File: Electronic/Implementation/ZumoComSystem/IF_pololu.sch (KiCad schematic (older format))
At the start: 35 parts, among them J4 Pin-Header 2x13, J5 Conn_02x07_Odd_Even, J6 Pin-Header 2x13, J7 Conn_02x07_Odd_Even, Q10 SI2302CDS-T1-BE3, Q6 SI2302CDS-T1-BE3, Q7 SI2302CDS-T1-BE3, Q8 SI2302CDS-T1-BE3, Q9 SI2302CDS-T1-BE3, SW3 KMR221GLFS, SW4 KMR221GLFS, SW5 KMR221GLFS

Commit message: #93 small fixes
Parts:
- D11: Manufacturer (none) -> Broadcom Limited; Part-No. (none) -> HSMF-C118
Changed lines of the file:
@@
 Sheet 7 7
 Title "Zumo Communication System"
-Date "2022-08-04"
+Date "2022-08-05"
 Rev "V1.1"
 Comp "NewTec GmbH"
@@
 F 2 "footprints:LED_RGB_1210" H 2800 6850 50  0001 C CNN
 F 3 "https://docs.broadcom.com/doc/AV02-0610EN" H 2800 6850 50  0001 C CNN
+F 4 "Broadcom Limited" H 2800 6900 50  0001 C CNN "Manufacturer"
+F 5 "HSMF-C118" H 2800 6900 50  0001 C CNN "Part-No."
 	1    2800 6900
 	1    0    0    -1

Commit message: #95 Anode of State-LED (D11) with 3V3 instead 5V connected
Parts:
- R28, R29: value 150 -> 100; Part-No. RC0603FR-07150RL -> RT0603FRE07100RL
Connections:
- net +3V3: now also D11.1 (A)
- net +5V: no longer D11.1 (A)
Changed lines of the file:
@@
 Sheet 7 7
 Title "Zumo Communication System"
-Date "2022-09-07"
+Date "2022-09-12"
 Rev "V1.2"
 Comp "NewTec GmbH"
@@
 Text HLabel 1400 7250 0    50   Input ~ 0
 nRGB_LED_B
-$Comp
-L Device:R R28
-U 1 1 61002789
-P 2100 6900
-F 0 "R28" V 1893 6900 50  0000 C CNN
-F 1 "150" V 1984 6900 50  0000 C CNN
-F 2 "Resistor_SMD:R_0603_1608Metric_Pad1.05x0.95mm_HandSolder" V 2030 6900 50  0001 C CNN
-F 3 "~" H 2100 6900 50  0001 C CNN
-F 4 "YAGEO" H 2100 6900 50  0001 C CNN "Manufacturer"
-F 5 "RC0603FR-07150RL" H 2100 6900 50  0001 C CNN "Part-No."
-	1    2100 6900
-	0    1    1    0
-$EndComp
-$Comp
-L Device:R R29
-U 1 1 61002936
-P 2100 7250
-F 0 "R29" V 1893 7250 50  0000 C CNN
-F 1 "150" V 1984 7250 50  0000 C CNN
-F 2 "Resistor_SMD:R_0603_1608Metric_Pad1.05x0.95mm_HandSolder" V 2030 7250 50  0001 C CNN
-F 3 "~" H 2100 7250 50  0001 C CNN
-F 4 "YAGEO" H 2100 7250 50  0001 C CNN "Manufacturer"
-F 5 "RC0603FR-07150RL" H 2100 7250 50  0001 C CNN "Part-No."
-	1    2100 7250
-	0    1    1    0
-$EndComp
 Wire Wire Line
 	2250 6550 2450 6550
@@
 $EndComp
 $Comp
-L power:+5V #PWR061
-U 1 1 6222DB21
-P 3250 6500
-F 0 "#PWR061" H 3250 6350 50  0001 C CNN
-F 1 "+5V" H 3265 6673 50  0000 C CNN
-F 2 "" H 3250 6500 50  0001 C CNN
-F 3 "" H 3250 6500 50  0001 C CNN
-	1    3250 6500
-	1    0    0    -1
-$EndComp
-$Comp
 L power:+5V #PWR072
 U 1 1 62267367
@@
 Wire Wire Line
 	2250 6900 2600 6900
-$Comp
-L Device:R R27
-U 1 1 61001F8A
-P 2100 6550
-F 0 "R27" V 1893 6550 50  0000 C CNN
-F 1 "300" V 1984 6550 50  0000 C CNN
-F 2 "Resistor_SMD:R_0603_1608Metric_Pad1.05x0.95mm_HandSolder" V 2030 6550 50  0001 C CNN
-F 3 "~" H 2100 6550 50  0001 C CNN
-F 4 "Bourns Inc." H 2100 6550 50  0001 C CNN "Manufacturer"
-F 5 "CR0603-JW-301ELF" H 2100 6550 50  0001 C CNN "Part-No."
-	1    2100 6550
-	0    1    1    0
-$EndComp
 Text Notes 5950 4150 0    50   ~ 0
 I_max = 2.6 A
@@
 Text Notes 9150 3200 0    50   ~ 0
 right
+$Comp
+L power:+3.3V #PWR?
+U 1 1 6320421B
+P 3250 6500
+F 0 "#PWR?" H 3250 6350 50  0001 C CNN
+F 1 "+3.3V" H 3265 6673 50  0000 C CNN
+F 2 "" H 3250 6500 50  0001 C CNN
+F 3 "" H 3250 6500 50  0001 C CNN
+	1    3250 6500
+	1    0    0    -1
+$EndComp
+$Comp
+L Device:R R27
+U 1 1 61001F8A
+P 2100 6550
+F 0 "R27" V 1893 6550 50  0000 C CNN
+F 1 "300" V 1984 6550 50  0000 C CNN
+F 2 "Resistor_SMD:R_0603_1608Metric_Pad1.05x0.95mm_HandSolder" V 2030 6550 50  0001 C CNN
+F 3 "~" H 2100 6550 50  0001 C CNN
+F 4 "Bourns Inc." H 2100 6550 50  0001 C CNN "Manufacturer"
+F 5 "CR0603-JW-301ELF" H 2100 6550 50  0001 C CNN "Part-No."
+	1    2100 6550
+	0    1    1    0
+$EndComp
+$Comp
+L Device:R R29
+U 1 1 61002936
+P 2100 7250
+F 0 "R29" V 1893 7250 50  0000 C CNN
+F 1 "100" V 1984 7250 50  0000 C CNN
+F 2 "Resistor_SMD:R_0603_1608Metric_Pad1.05x0.95mm_HandSolder" V 2030 7250 50  0001 C CNN
+F 3 "~" H 2100 7250 50  0001 C CNN
+F 4 "YAGEO" H 2100 7250 50  0001 C CNN "Manufacturer"
+F 5 "RT0603FRE07100RL" H 2100 7250 50  0001 C CNN "Part-No."
+	1    2100 7250
+	0    1    1    0
+$EndComp
+$Comp
+L Device:R R28
+U 1 1 61002789
+P 2100 6900
+F 0 "R28" V 1893 6900 50  0000 C CNN
+F 1 "100" V 1984 6900 50  0000 C CNN
+F 2 "Resistor_SMD:R_0603_1608Metric_Pad1.05x0.95mm_HandSolder" V 2030 6900 50  0001 C CNN
+F 3 "~" H 2100 6900 50  0001 C CNN
+F 4 "YAGEO" H 2100 6900 50  0001 C CNN "Manufacturer"
+F 5 "RT0603FRE07100RL" H 2100 6900 50  0001 C CNN "Part-No."
+	1    2100 6900
+	0    1    1    0
+$EndComp
 $EndSCHEMATC

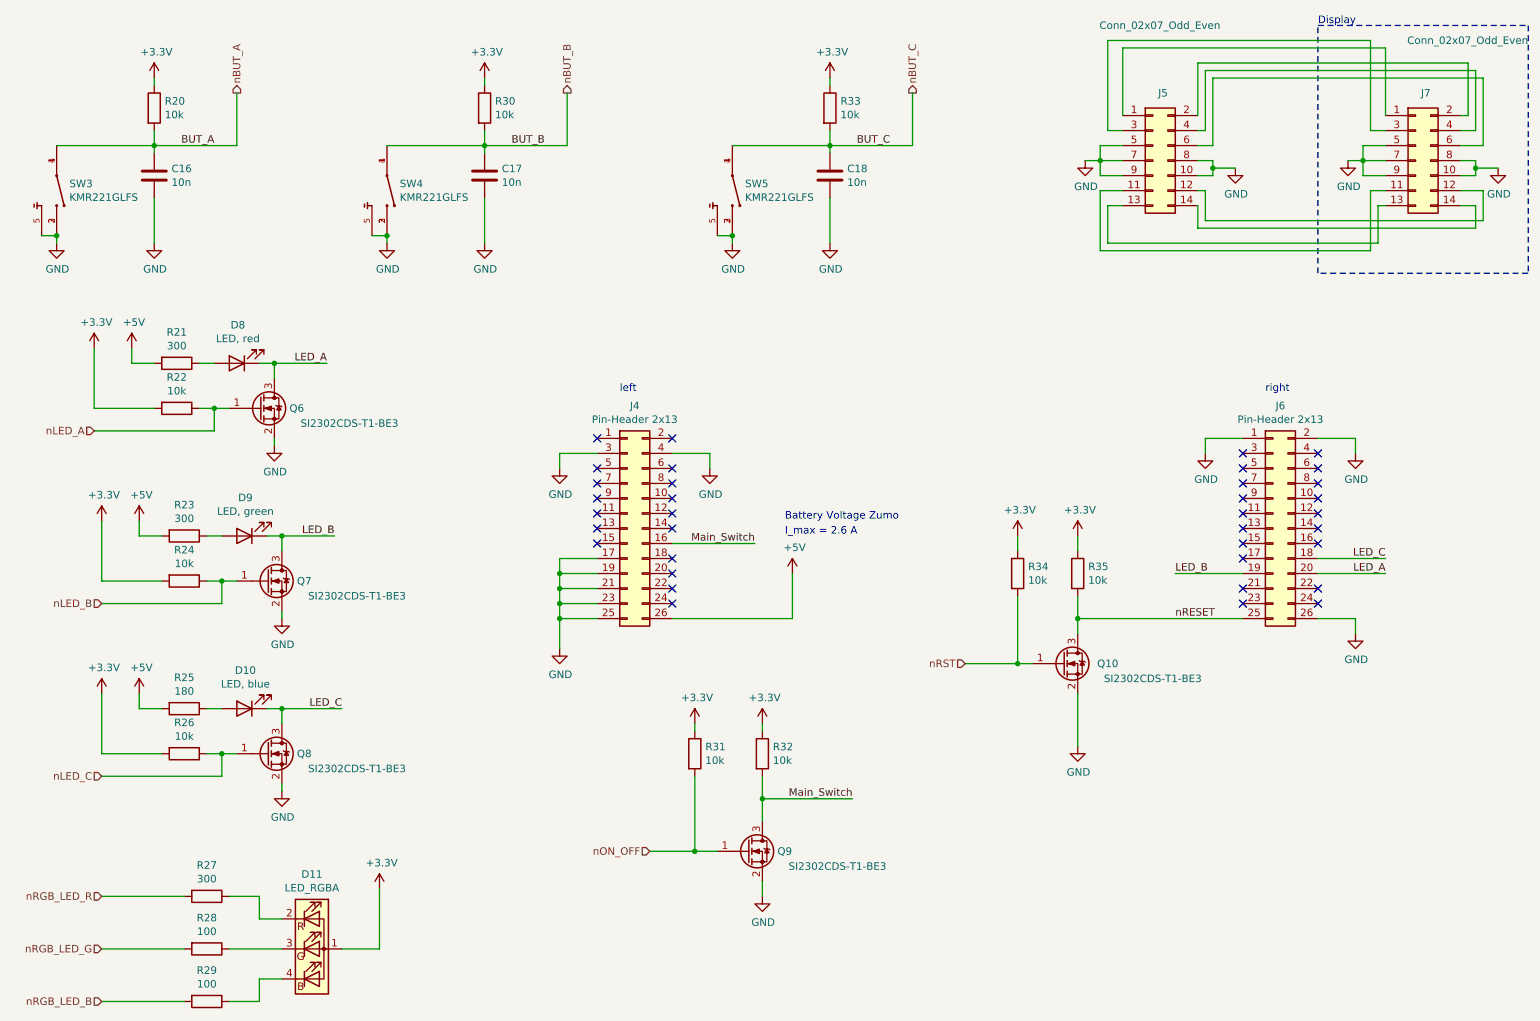
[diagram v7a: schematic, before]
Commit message: #95 LED and Pinning - Pinning updated (LEDs, Buttons, Measurement) - LEDs adapted/edited (color, order, ...) - connections to ZumoRobot removed
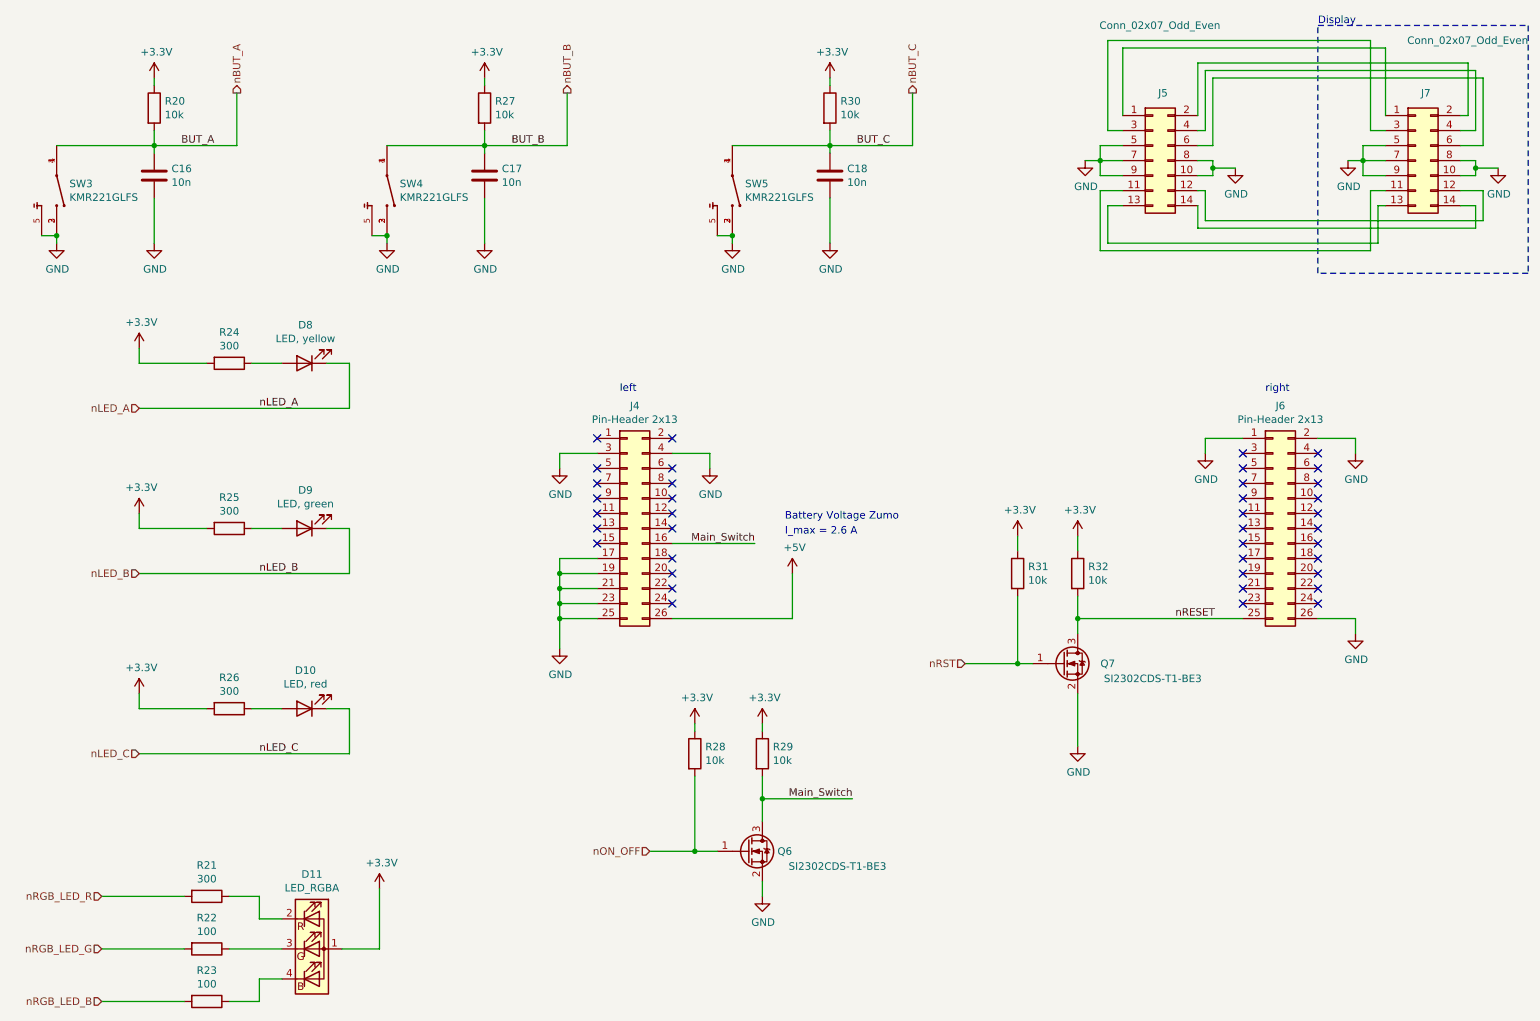
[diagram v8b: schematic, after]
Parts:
- removed Q6, Q7, Q8: SI2302CDS-T1-BE3, Package_TO_SOT_SMD:SOT-23, symbol Device:Q_NMOS_GSD
- removed R21, R23: 300, Resistor_SMD:R_0603_1608Metric_Pad1.05x0.95mm_HandSolder, symbol Device:R
- removed R22, R26: 10k, Resistor_SMD:R_0603_1608Metric_Pad1.05x0.95mm_HandSolder, symbol Device:R
- added R25: 300, Resistor_SMD:R_0603_1608Metric_Pad1.05x0.95mm_HandSolder, symbol Device:R
- D8: renamed from D10; value LED, blue -> LED, yellow; Part-No. 150060BS55040 -> 150060YS55040
- R24: value 10k -> 300; Manufacturer TE Connectivity Passive Product -> Bourns Inc.; Part-No. CRGCQ0603J10K -> CR0603-JW-301ELF
- R26: renamed from R25; value 180 -> 300; Manufacturer TE Connectivity Passive Product -> Bourns Inc.; Part-No. CRGP0603F180R -> CR0603-JW-301ELF
- renumbered D8 to D10, Q9 to Q6, Q10 to Q7, R27 to R21, R28 to R22, R29 to R23, R30 to R27, R31 to R28, R32 to R29, R33 to R30, R34 to R31, R35 to R32
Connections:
- net +3V3: now also R26.2, R25.2
- net +5V: no longer R26.2
- net nLED_A: now also D8.1 (K)
- net nLED_B: now also D9.1 (K); no longer R24.1
- net nLED_C: now also D10.1 (K)
- net at D9.2 (A): now also R25.1
- net at D10.2 (A): now also R26.1
- net at D8.2 (A): now also R24.1; no longer R26.1
- net LED_A: no longer names the net of J6.20 (Pin_20)
- net LED_A: no longer D10.1 (K)
- net LED_B: no longer names the net of J6.19 (Pin_19)
- net LED_B: no longer D9.1 (K)
- net LED_C: no longer names the net of J6.18 (Pin_18)
- net LED_C: no longer D8.1 (K)
- no-connect marks 36 -> 39
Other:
- moved on the sheet: D10, D8, D9, R26
